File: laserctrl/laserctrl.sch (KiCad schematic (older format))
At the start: 17 parts

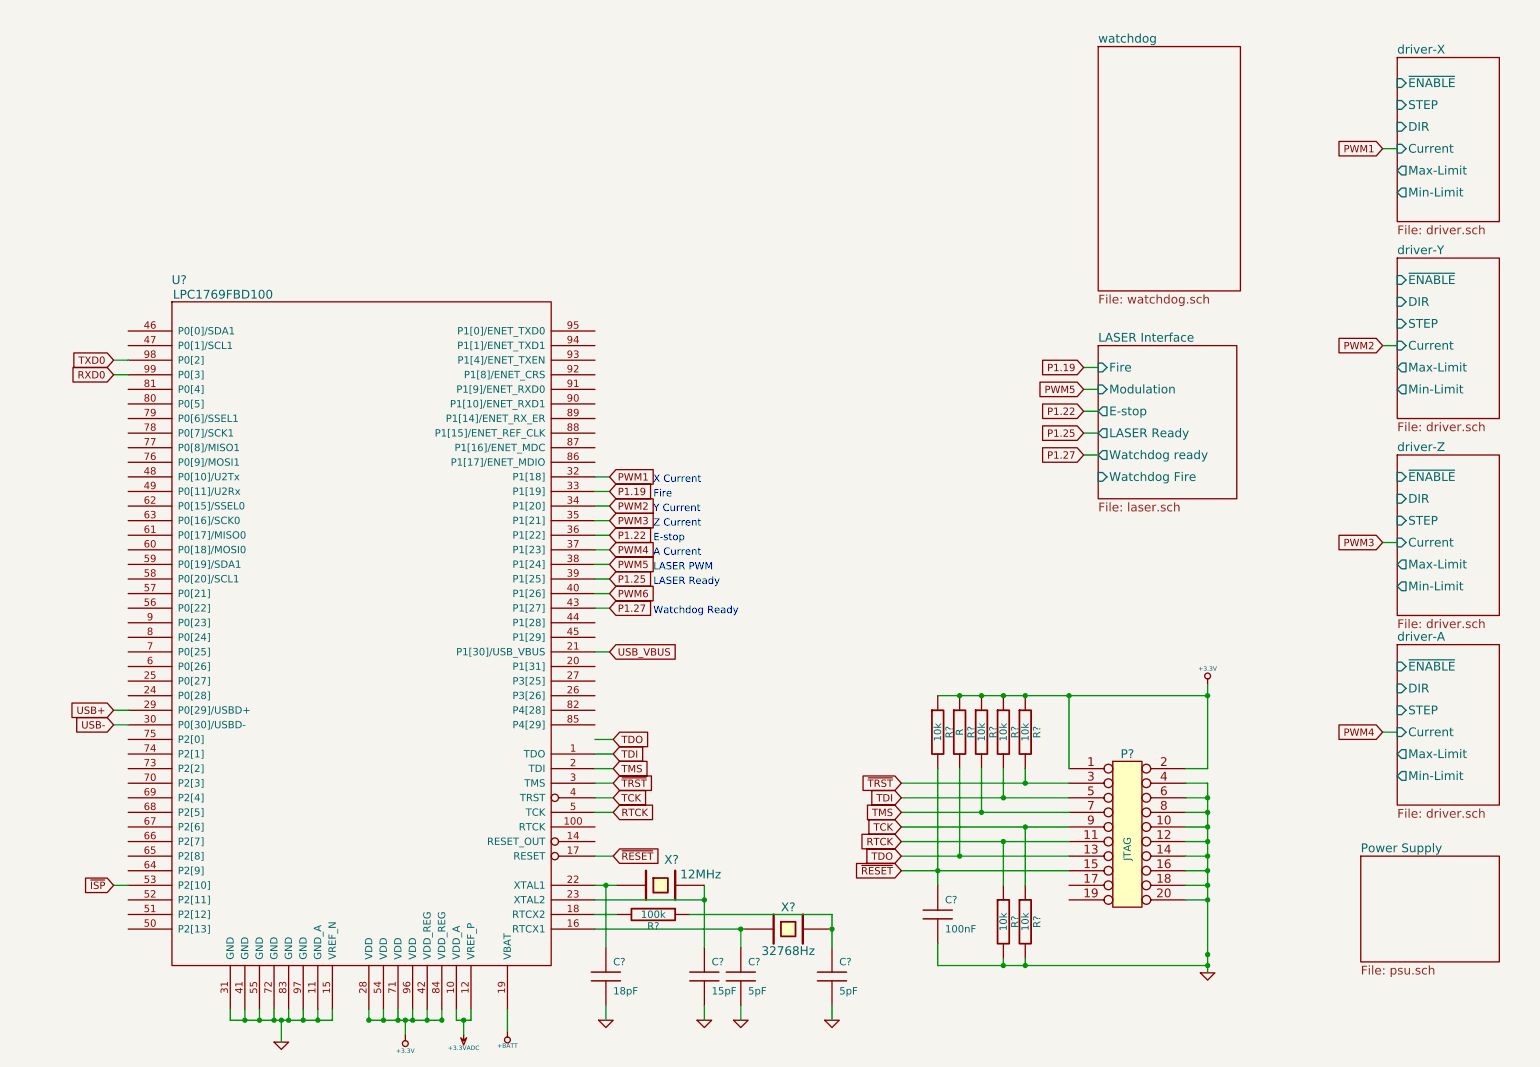
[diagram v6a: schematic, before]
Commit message: Added NTC sensors
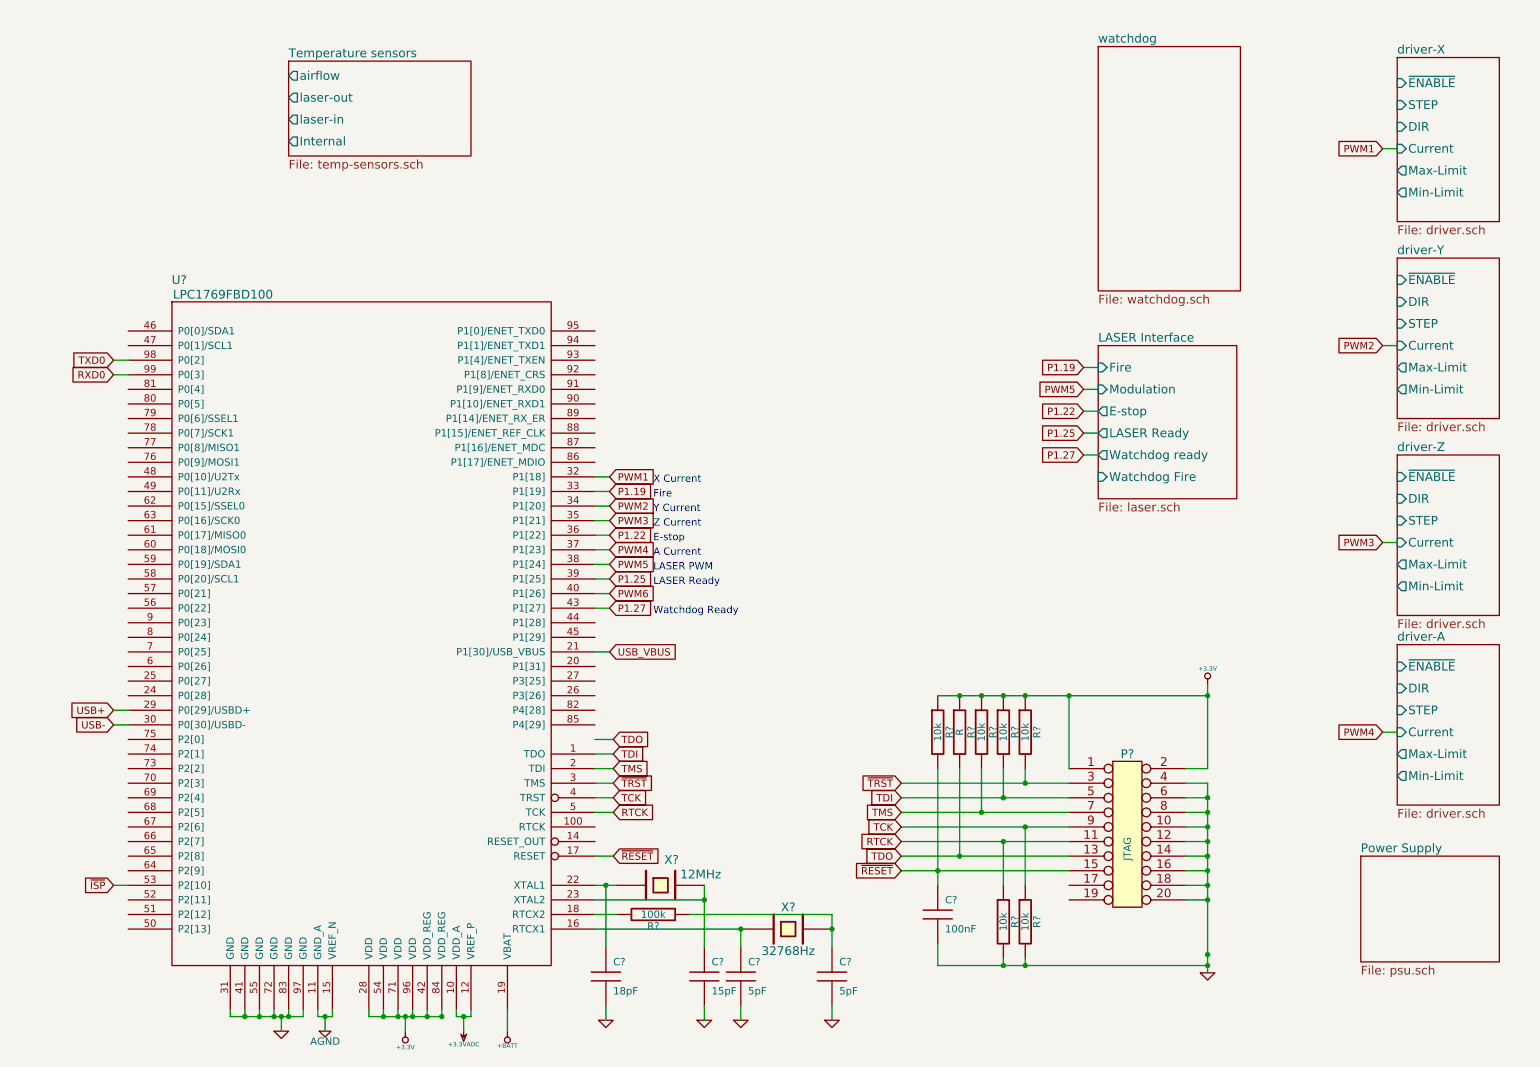
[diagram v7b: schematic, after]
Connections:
- net GND: no longer U?.11 (GND_A), U?.15 (VREF_N)
- new net AGND: U?.11 (GND_A), U?.15 (VREF_N)

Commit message: Added the chiller and the USB/Serial/ISP/SD subsystems and added some specs on the chiller protocol
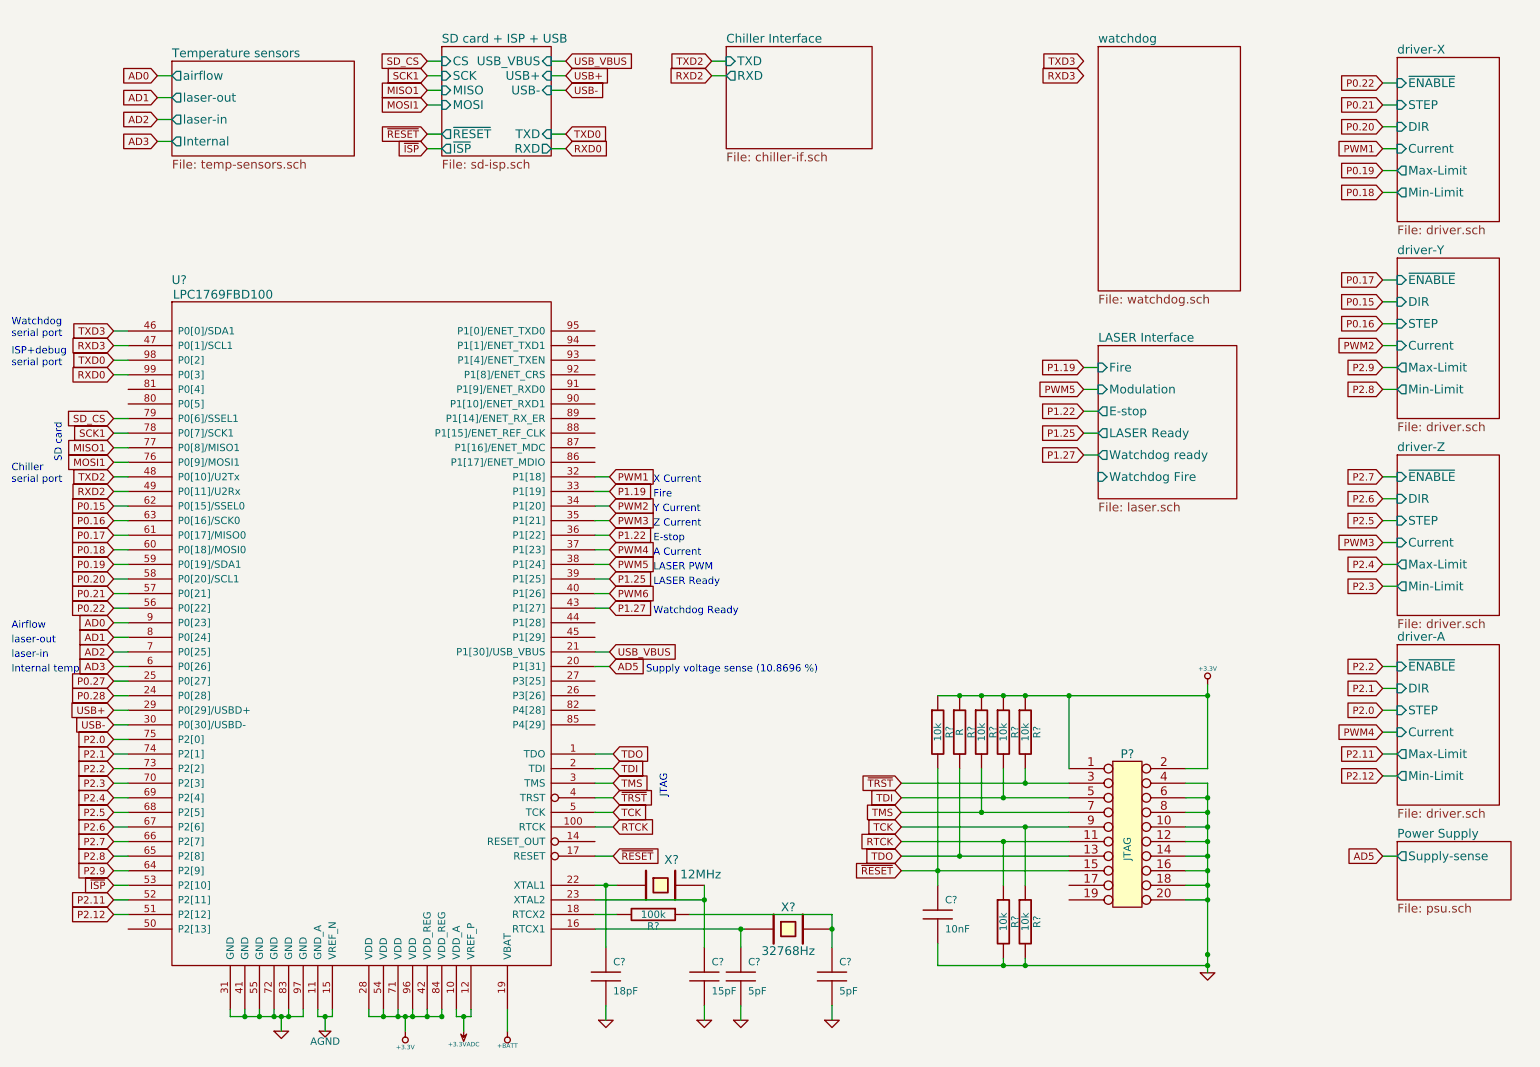
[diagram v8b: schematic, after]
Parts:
- C?: value 100nF -> 10nF
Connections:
- net RTCK: now also U?.100 (RTCK); no longer U?.5 (TCK)
- net TCK: now also U?.5 (TCK); no longer U?.4 (TRST)
- net TDI: now also U?.2 (TDI); no longer U?.1 (TDO)
- net TDO: now also U?.1 (TDO)
- net TMS: now also U?.3 (TMS); no longer U?.2 (TDI)
- net ~TRST: now also U?.4 (TRST); no longer U?.3 (TMS)
- net AD5: now reaches U?.20 (P1[31])
- net P0.28: now reaches U?.24 (P0[28])
- net P0.27: now reaches U?.25 (P0[27])
- net TXD3: now reaches U?.46 (P0[0]/SDA1)
- net RXD3: now reaches U?.47 (P0[1]/SCL1)
- net TXD2: now reaches U?.48 (P0[10]/U2Tx)
- net RXD2: now reaches U?.49 (P0[11]/U2Rx)
- net P2.12: now reaches U?.51 (P2[12])
- net P2.11: now reaches U?.52 (P2[11])
- net P0.22: now reaches U?.56 (P0[22])
- net P0.21: now reaches U?.57 (P0[21])
- net P0.20: now reaches U?.58 (P0[20]/SCL1)
- net P0.19: now reaches U?.59 (P0[19]/SDA1)
- net AD3: now reaches U?.6 (P0[26])
- net P0.18: now reaches U?.60 (P0[18]/MOSI0)
- net P0.17: now reaches U?.61 (P0[17]/MISO0)
- net P0.15: now reaches U?.62 (P0[15]/SSEL0)
- net P0.16: now reaches U?.63 (P0[16]/SCK0)
- net P2.9: now reaches U?.64 (P2[9])
- net P2.8: now reaches U?.65 (P2[8])
- net P2.7: now reaches U?.66 (P2[7])
- net P2.6: now reaches U?.67 (P2[6])
- net P2.5: now reaches U?.68 (P2[5])
- net P2.4: now reaches U?.69 (P2[4])
- net AD2: now reaches U?.7 (P0[25])
- net P2.3: now reaches U?.70 (P2[3])
- net P2.2: now reaches U?.73 (P2[2])
- net P2.1: now reaches U?.74 (P2[1])
- net P2.0: now reaches U?.75 (P2[0])
- net MOSI1: now reaches U?.76 (P0[9]/MOSI1)
- net MISO1: now reaches U?.77 (P0[8]/MISO1)
- net SCK1: now reaches U?.78 (P0[7]/SCK1)
- net SD_CS: now reaches U?.79 (P0[6]/SSEL1)
- net AD1: now reaches U?.8 (P0[24])
- net AD0: now reaches U?.9 (P0[23])
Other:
- note added: "Airflow"
- note added: "Chiller\nserial port"
- note added: "ISP+debug\nserial port"
- note added: "Internal temp"
- note added: "JTAG"
- note added: "SD card\n"
- note added: "Supply voltage sense (10.8696 %)"
- note added: "Watchdog\nserial port"
- note added: "laser-in"
- note added: "laser-out"
